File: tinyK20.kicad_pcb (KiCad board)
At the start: 2 copper layers, 45.8 x 73.7 mm, 78 parts, among them CON1 USB-MINI-B, P1 CONN_1, P10 CONN_1, P11 CONN_1, P12 CONN_1, P13 CONN_1, P14 CONN_1, P15 CONN_1, P16 CONN_1, P17 CONN_1, P18 CONN_1, P19 CONN_1, P2 CONN_1, P20 CONN_1, P21 CONN_1, P22 CONN_1, P23 CONN_1, P24 CONN_1, P25 CONN_1, P26 CONN_1, P27 CONN_1, P28 CONN_1, P29 CONN_1, P3 CONN_1, P30 CONN_1, P31 CONN_1, P32 CONN_1, P33 CONN_1, P34 CONN_1, P35 CONN_5X2, P36 CONN_1, P37 CONN_1, P38 CONN_5X2, P4 CONN_1, P41 CONN_1, P5 CONN_1, P6 CONN_1, P7 CONN_1, P8 CONN_1, P9 CONN_1, SW1 SW_PUSH, U1 MK20DX128VFT5, U2 LT1129CST-3.3, U3 74LS126, X3 MOLEX-MICRO-SD, Y1 Crystal, Y2 Crystal_Small

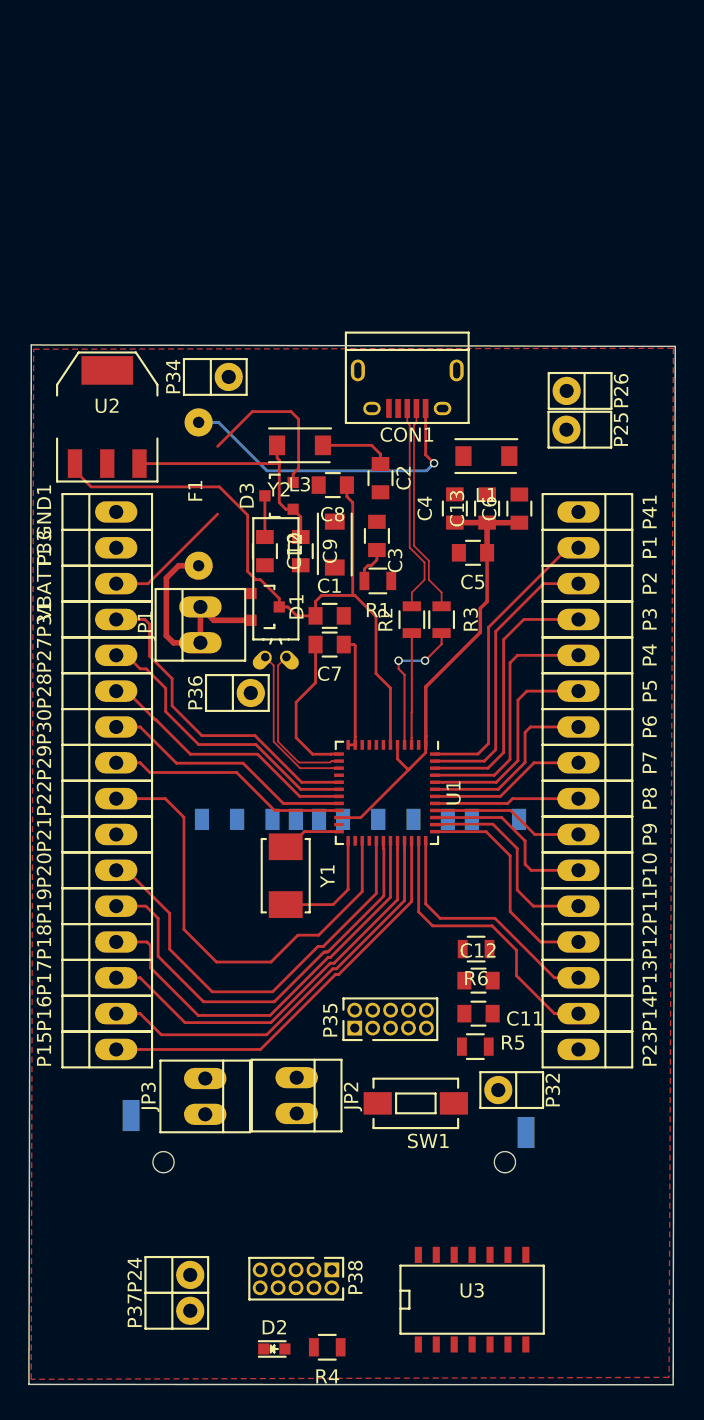
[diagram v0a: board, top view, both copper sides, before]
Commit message: Simplify the board
Remove all breakout pin headers
remove SD card connector
redo the PCB layout
change the debug connector to through hole 1.27mm
change the resistor footprints to handsoldering ones
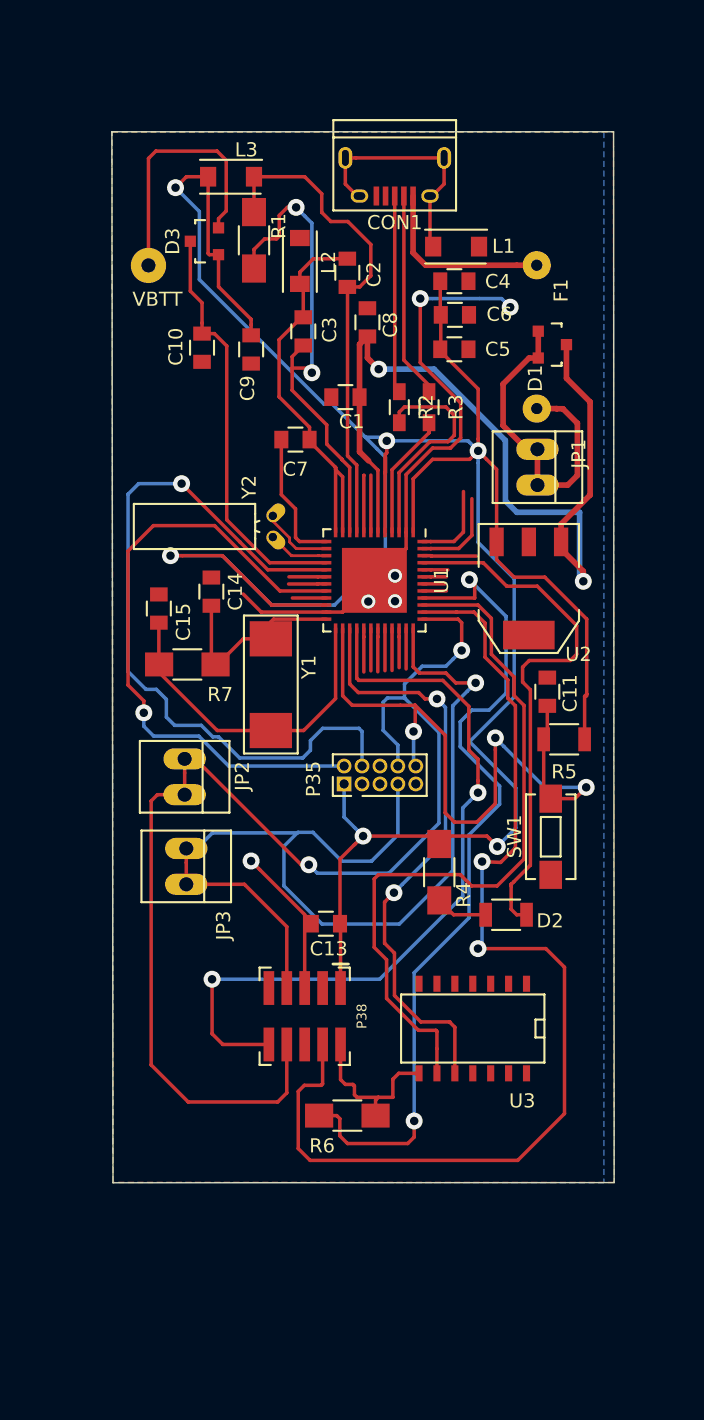
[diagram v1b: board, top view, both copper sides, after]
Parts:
- removed C12: 2.2u, Capacitors_SMD:C_0805
- removed GND1, P1, P10, P11, P12, P13, P14, P15, P16, P17, P18, P19, P2, P20, P21, P22, P23, P27, P28, P29, P3, P30, P31, P33, P4, P41, P5, P6, P7, P8, P9, VBATT1: CONN_1, Connect:PIN1
- removed P24, P25, P26, P32, P34, P36, P37: CONN_1, Connect:PINC
- removed X3: MOLEX-MICRO-SD, Connect:SD_Card_Receptacle
- added C14: 22nF, Capacitors_SMD:C_0805, F.Cu at (63.2, 61.9)
- added C15: 22nF, Capacitors_SMD:C_0805, F.Cu at (59.5, 63.1)
- added R7: 1M, Resistors_SMD:R_1206_HandSoldering, F.Cu at (61.5, 67.1)
- added VBTT: CONN_1, Wire_Pads:SolderWirePad_single_1mmDrill, F.Cu at (58.8, 38.8)
- D2: footprint LEDs:LED_0603 -> Resistors_SMD:R_1206
- P38: footprint Pin_Headers:Pin_Header_Straight_2x05_Pitch1.27mm -> Connect:CONN-2x5-1.27-SMT
- R1, R4, R6: footprint Resistors_SMD:R_0805 -> Resistors_SMD:R_1206_HandSoldering
- R2, R3: footprint Resistors_SMD:R_0805 -> Resistors_SMD:R_0603_HandSoldering
- R5: footprint Resistors_SMD:R_0805 -> Resistors_SMD:R_1206
- Y1: footprint Crystals:ABM3 -> Housings_DFN_QFN:ABM3
- moved D2 34.9 mm to (84.1, 84.8)
- moved R4 34.6 mm to (79.4, 81.8), turned to 270 degrees
- moved U2 32.3 mm to (85.7, 61.7), turned to 180 degrees
- moved C13 31.6 mm to (71.4, 85.5), turned to 180 degrees
- moved D1 27.6 mm to (87.4, 44.4)
- moved F1 26.4 mm to (86.3, 38.8)
- moved JP1 26.4 mm to (86.3, 53.1), turned to 270 degrees
- moved R1 25.7 mm to (66.3, 37.0), turned to 270 degrees
- moved JP2 24.0 mm to (61.3, 75.1)
- moved C11 23.3 mm to (87.0, 69.0), turned to 90 degrees
- moved R5 22.7 mm to (88.2, 72.4), turned to 180 degrees
- moved SW1 21.2 mm to (87.3, 79.3), turned to 90 degrees
- moved L2 20.3 mm to (69.5, 38.5), turned to 270 degrees
- moved L3 19.7 mm to (64.6, 32.5)
- moved U3 19.0 mm to (81.8, 93.0), turned to 180 degrees
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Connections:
- JP2 pad 1: Net-(JP2-Pad1) -> UART1_TX
- JP3 pad 1: Net-(JP3-Pad1) -> UART1_RX
- P38 pad 3: Net-(P38-Pad3) -> GND
- P38 pad 5: Net-(P38-Pad3) -> GND
- U1 pad 18: Net-(P27-Pad1) -> (no net)
- U1 pad 19: Net-(P28-Pad1) -> (no net)
- U1 pad 21: Net-(P29-Pad1) -> (no net)
- U1 pad 29: Net-(P20-Pad1) -> (no net)
- U1 pad 30: Net-(P19-Pad1) -> (no net)
- U1 pad 31: Net-(P18-Pad1) -> (no net)
- U1 pad 32: Net-(P17-Pad1) -> (no net)
- U1 pad 33: PTC0 -> (no net)
- U1 pad 34: PTC1 -> (no net)
- U1 pad 35: Net-(P14-Pad1) -> (no net)
- U1 pad 36: Net-(JP3-Pad1) -> UART1_RX
- U1 pad 37: Net-(JP2-Pad1) -> UART1_TX
- U1 pad 41: Net-(P8-Pad1) -> (no net)
- U1 pad 42: Net-(P7-Pad1) -> (no net)
- U1 pad 43: Net-(P6-Pad1) -> (no net)
- U1 pad 44: Net-(P5-Pad1) -> (no net)
- U1 pad 46: Net-(P3-Pad1) -> (no net)
- U1 pad 47: Net-(P2-Pad1) -> (no net)
- U1 pad 48: Net-(P1-Pad1) -> (no net)
- U1 pad 7: Net-(P25-Pad1) -> (no net)
- U1 pad 8: Net-(P26-Pad1) -> (no net)
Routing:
- net 3V3: track 50.4 -> 200.1 mm, vias 0 -> 6
- net UART1_TX: track 0.00 -> 88.4 mm, vias 0 -> 2
- net UART1_RX: track 0.00 -> 76.4 mm, vias 0 -> 1
- net PTC5: track 14.3 -> 77.3 mm, vias 0 -> 2
- net (no net): track 0.00 -> 59.9 mm
- net GND: track 0.00 -> 57.8 mm, vias 0 -> 6
- net PTB1: track 0.00 -> 54.9 mm, vias 0 -> 2
- net RESET: track 0.00 -> 50.6 mm, vias 0 -> 3
- net PTC7: track 10.9 -> 59.9 mm, vias 0 -> 2
- net SWD_CLK: track 11.6 -> 53.1 mm, vias 0 -> 1
- net PTC6: track 12.7 -> 51.5 mm
- net Net-(C3-Pad1): track 2.70 -> 35.4 mm, vias 0 -> 2
- net Net-(C2-Pad1): track 5.04 -> 35.5 mm
- net Net-(P19-Pad1): track 30.4 -> 0.00 mm
- net Net-(P20-Pad1): track 30.1 -> 0.00 mm
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- added copper zone on B.Cu, net GND
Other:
- board size 45.8 x 73.7 mm -> 35.6 x 74.5 mm
- net class Default: trace_width 0.4 -> 0.25; via_dia 0.6 -> 1.2; via_drill 0.4 -> 0.6
- net class diff: clearance 0.1 -> 0.2; via_dia 0.4 -> 1.2; via_drill 0.3 -> 0.6
- rule trace_min: 0.1 -> 0.006
- rule via_min_drill: 0.3 -> 0.013
- rule via_min_size: 0.4 -> 0.027

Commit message: Add breakout headers and reroute the whole PCB board
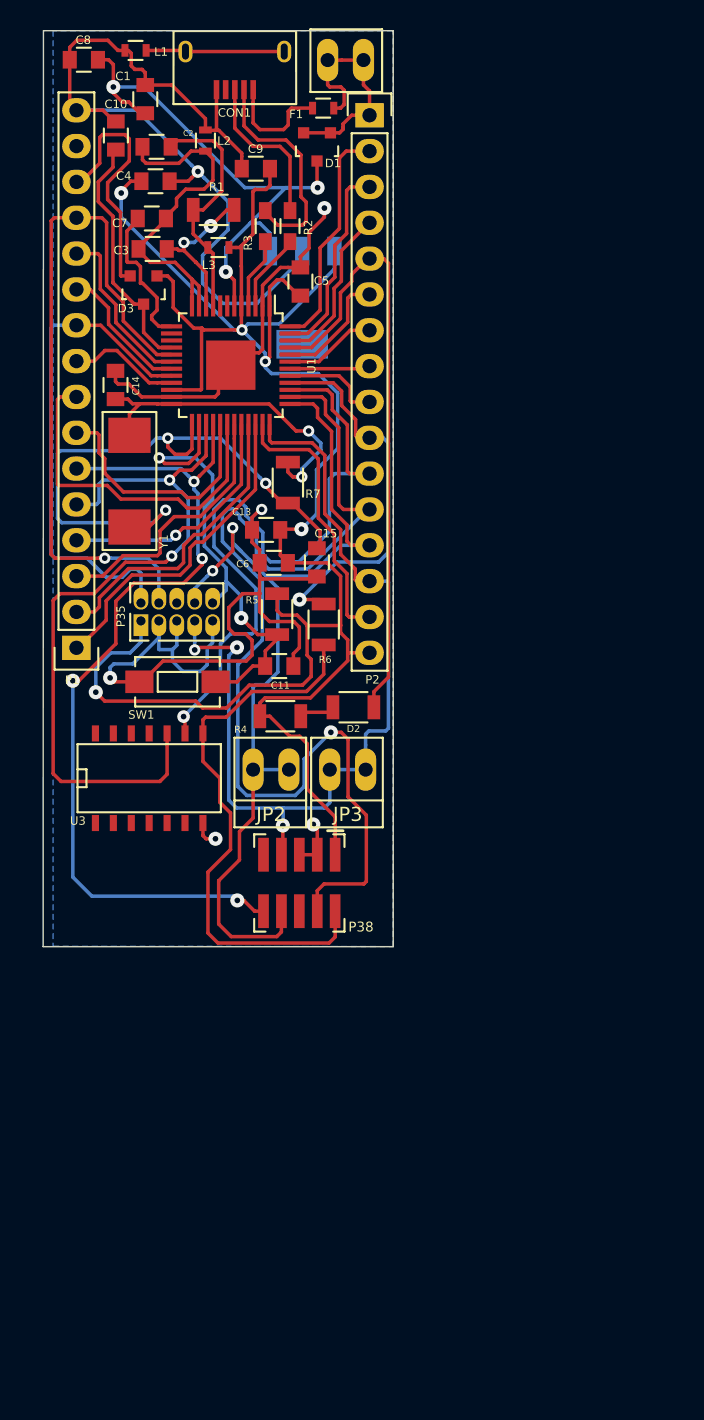
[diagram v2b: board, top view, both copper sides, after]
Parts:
- removed VBTT: CONN_1, Wire_Pads:SolderWirePad_single_1mmDrill
- removed Y2: Crystal_Small, Crystals:Crystal_Round_Horizontal_3mm_BigPad
- added P1: CONN_01X16, Pin_Headers:Pin_Header_Straight_1x16, F.Cu at (53.7, 65.9)
- added P2: CONN_01X16, Pin_Headers:Pin_Header_Straight_1x16, F.Cu at (74.4, 28.2)
- C10: value 100n -> C
- CON1: value USB-MINI-B -> USB-MICRO-B
- F1: footprint Wire_Connections_Bridges:WireConnection_0.80mmDrill -> Resistors_SMD:R_0603
- L1, L2, L3: footprint Inductors_NEOSID:Neosid_Inductor_SM1206 -> Resistors_SMD:R_0603
- P38: footprint Connect:CONN-2x5-1.27-SMT -> Pin_Headers:CONN-2x5-1.27-SMT
- R1, R4, R6, R7: footprint Resistors_SMD:R_1206_HandSoldering -> Resistors_SMD:R_1206
- U1: footprint Housings_DFN_QFN:QFN-48-1EP_7x7mm_Pitch0.5mm -> Housings_QFP:TQFP-48-1EP_7x7mm_Pitch0.5mm
- U2: moved to B.Cu
- moved R6 34.8 mm to (71.2, 64.3), turned to 270 degrees
- moved JP1 31.9 mm to (72.7, 24.3), turned to 0 degrees
- moved U3 29.2 mm to (58.8, 75.0), turned to 0 degrees
- moved SW1 28.6 mm to (60.8, 68.3), turned to 0 degrees
- moved C13 28.2 mm to (67.1, 57.6)
- moved C8 27.4 mm to (54.2, 24.2), turned to 180 degrees
- moved L1 26.6 mm to (57.9, 23.6), turned to 0 degrees
- moved U2 26.1 mm to (69.7, 41.1), turned to 0 degrees
- moved C1 25.4 mm to (58.5, 27.0), turned to 90 degrees
- moved C4 22.3 mm to (59.3, 32.8)
- moved R5 22.2 mm to (67.9, 63.5), turned to 270 degrees
- moved D1 21.8 mm to (70.7, 30.4), turned to 180 degrees
- moved C6 21.8 mm to (67.7, 59.9), turned to 180 degrees
- moved C11 19.1 mm to (68.0, 67.2), turned to 0 degrees
- moved F1 18.8 mm to (71.2, 27.7), turned to 0 degrees
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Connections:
- net /D+ renamed D+
- net /D- renamed D-
- net LED renamed PTD4
- net Net-(D1-Pad1) renamed 5V
- net SWD_CLK renamed PTA0
- net SWD_IO renamed PTA3
- D3 pad 2: Net-(D3-Pad2) -> VBATT
- U1 pad 14: /xtal_P -> (no net)
- U1 pad 15: /xtal_N -> (no net)
- U1 pad 18: (no net) -> PTA1
- U1 pad 19: (no net) -> PTA2
- U1 pad 21: (no net) -> PTA4
- U1 pad 29: (no net) -> PTB2
- U1 pad 30: (no net) -> PTB3
- U1 pad 31: (no net) -> PTB16
- U1 pad 32: (no net) -> PTB17
- U1 pad 33: (no net) -> PTC0
- U1 pad 34: (no net) -> PTC1
- U1 pad 35: (no net) -> PTC2
- U1 pad 41: (no net) -> PTD0
- U1 pad 42: (no net) -> PTD1
- U1 pad 43: (no net) -> PTD2
- U1 pad 44: (no net) -> PTD3
- U1 pad 46: (no net) -> PTD5
- U1 pad 47: (no net) -> PTD6
- U1 pad 48: (no net) -> PTD7
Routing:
- net GND: track 57.8 -> 150.8 mm
- net (no net): track 59.9 -> 0.00 mm
- net 3V3: track 200.1 -> 153.0 mm, vias 6 -> 5
- net PTC7: track 59.9 -> 27.3 mm, vias 2 -> 1
- net Net-(P38-Pad2): track 11.8 -> 39.9 mm
- net PTB3: track 0.00 -> 24.9 mm
- net Net-(C3-Pad1): track 35.4 -> 10.9 mm
- net PTC1: track 0.00 -> 23.6 mm
- net Vregin: track 62.2 -> 39.5 mm, vias 2 -> 3
- net PTC0: track 0.00 -> 21.6 mm
- net /x+: track 23.7 -> 43.5 mm, vias 0 -> 3
- net PTC2: track 0.00 -> 19.3 mm
- net PTB16: track 0.00 -> 19.1 mm
- net Net-(D3-Pad2): track 18.6 -> 0.00 mm
- net Net-(C2-Pad1): track 35.5 -> 17.0 mm
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- removed copper zone on F.Cu, net GND
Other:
- board size 35.6 x 74.5 mm -> 24.8 x 64.9 mm
- net class Default: via_dia 1.2 -> 0.6; via_drill 0.6 -> 0.4
- net class diff removed
- rule trace_min: 0.006 -> 0.2
- rule via_min_drill: 0.013 -> 0.3
- rule via_min_size: 0.027 -> 0.4

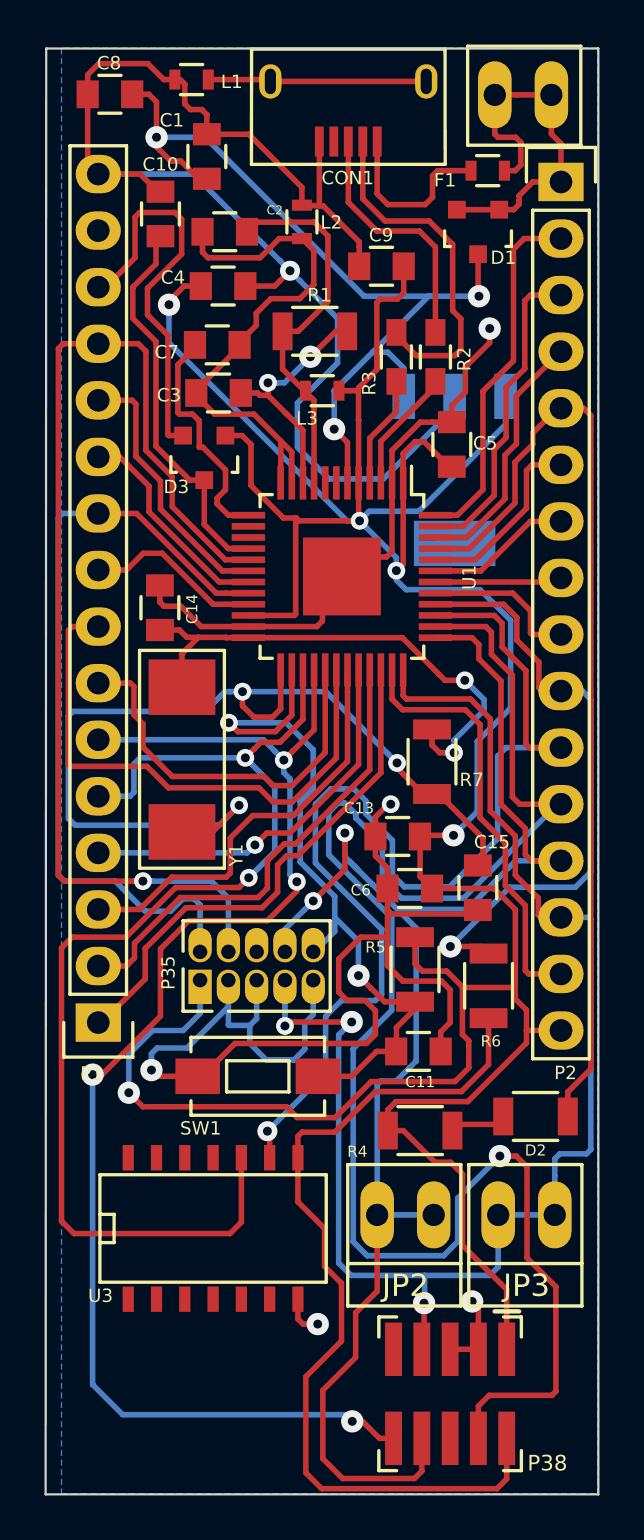
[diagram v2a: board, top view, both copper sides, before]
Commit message: Make the board smaller
Switch the ABM2 crystal with a smaller Murata CSTE
Switch the debug line driver chip with a smaller footprint one
Adjust pin headers hopefully to breadboard friendly
Remove Jumpers on UART lines
Remove the 1Mohm resistor and two capacitors for the crystal. Not needed
Resize the entire board downwards and re-route the traces
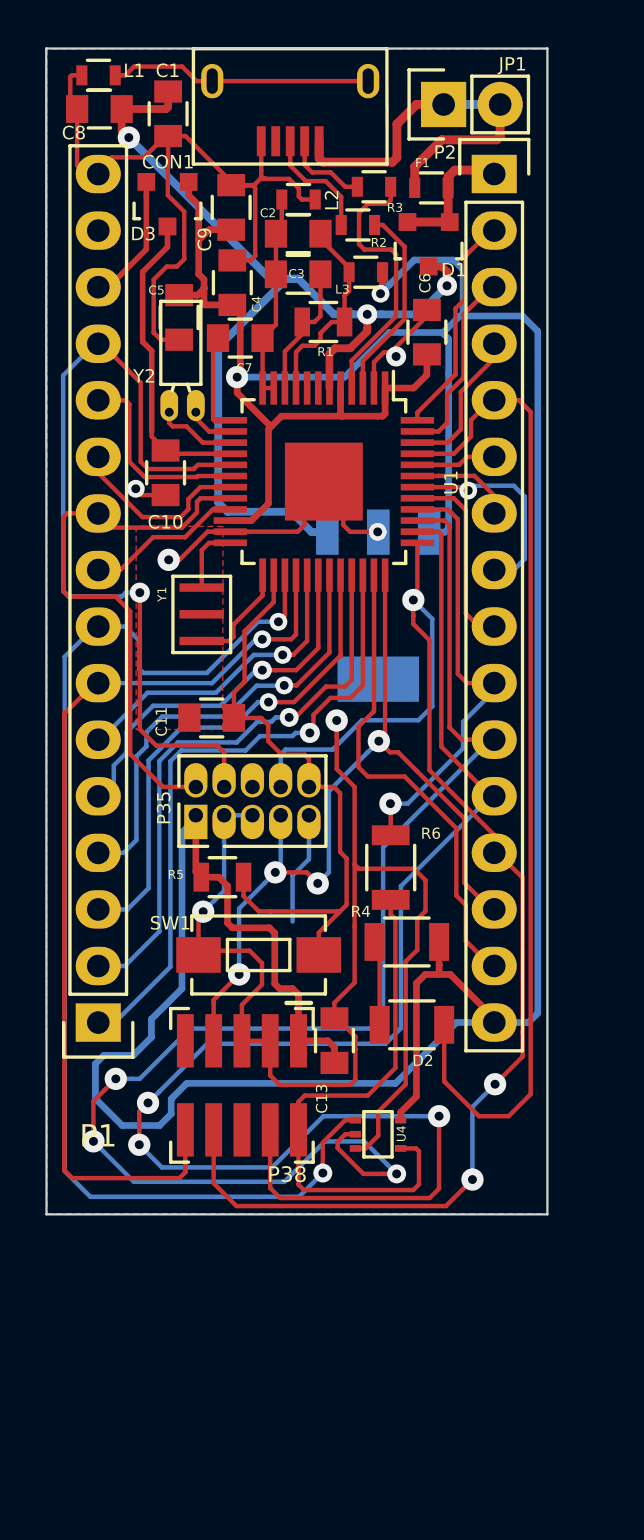
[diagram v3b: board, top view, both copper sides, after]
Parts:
- removed C14, C15: 22nF, Capacitors_SMD:C_0805
- removed JP2, JP3: JUMPER_F, Connect:PINHEAD1-2
- removed R7: 1M, Resistors_SMD:R_1206
- removed U3: 74LS126, SMD_Packages:SOIC-14_N
- added U4: 74AHC1G125, TO_SOT_Packages_SMD:SOT-353, F.Cu at (66.2, 70.9)
- added Y2: 32.768kHz, Crystals:Crystal_Round_Horizontal_2mm, F.Cu at (57.4, 38.5)
- C10: value C -> 100nF
- JP1: footprint Connect:PINHEAD1-2 -> Pin_Headers:Pin_Header_Straight_1x02
- R1, R5: footprint Resistors_SMD:R_1206 -> Resistors_SMD:R_0805
- R2, R3: footprint Resistors_SMD:R_0603_HandSoldering -> Resistors_SMD:R_0603
- Y1: value Crystal -> 8MHz; footprint Housings_DFN_QFN:ABM3 -> Crystals:CERALOCK-CSTCE8M00G15L99-R0
- moved C6 25.0 mm to (68.4, 34.9), turned to 90 degrees
- moved C11 17.6 mm to (58.8, 52.2), turned to 180 degrees
- moved P38 16.7 mm to (60.1, 68.7)
- moved C5 13.5 mm to (57.3, 34.3), turned to 270 degrees
- moved C10 11.6 mm to (56.7, 41.2), turned to 270 degrees
- moved D3 11.5 mm to (56.8, 29.2)
- moved C13 9.60 mm to (64.3, 66.7), turned to 90 degrees
- moved R5 9.59 mm to (59.2, 59.4), turned to 0 degrees
- moved R4 8.49 mm to (67.5, 62.3), turned to 180 degrees
- moved R3 7.71 mm to (66.1, 28.4), turned to 0 degrees
- moved P35 7.41 mm to (58.1, 56.6)
- moved C9 7.25 mm to (59.6, 29.3), turned to 90 degrees
- moved U2 6.99 mm to (66.2, 47.2)
- moved D2 6.91 mm to (67.8, 66.0)
- moved R6 6.89 mm to (66.8, 59.0)
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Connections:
- JP1 pad 1: 5V -> Vreg
- JP1 pad 2: 5V -> Vreg
- P1 pad 3: PTB16 -> PTB17
- P1 pad 4: PTB17 -> PTB16
- P1 pad 5: PTB0 -> PTB3
- P1 pad 6: PTB1 -> PTB2
- P1 pad 7: PTB2 -> PTB1
- P1 pad 8: PTB3 -> PTB0
- U1 pad 14: (no net) -> Net-(U1-Pad14)
- U1 pad 15: (no net) -> Net-(U1-Pad15)
- Y1 pad 2: /x+ -> GND
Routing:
- net /x+: track 43.5 -> 4.81 mm, vias 3 -> 0
- net GND: track 150.8 -> 120.6 mm
- net UART1_RX: track 64.3 -> 38.6 mm, vias 3 -> 4
- net /x-: track 23.2 -> 3.10 mm, vias 2 -> 0
- net PTB1: track 62.4 -> 42.6 mm, vias 4 -> 1
- net Net-(P38-Pad2): track 39.9 -> 24.3 mm
- net Net-(C2-Pad2): track 24.7 -> 9.33 mm
- net PTC6: track 50.0 -> 63.9 mm, vias 1 -> 3
- net PTA0: track 50.2 -> 37.8 mm
- net D-: track 15.8 -> 3.83 mm
- net VBATT: track 17.7 -> 5.89 mm
- net 5V: track 17.0 -> 6.40 mm
- net PTA3: track 35.8 -> 25.4 mm
- net 3V3: track 153.0 -> 162.9 mm, vias 5 -> 2
- net Vreg: track 7.96 -> 17.7 mm
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- added copper zone on F.Cu, net GND
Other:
- board size 24.8 x 64.9 mm -> 22.5 x 52.3 mm
- net class Default: clearance 0.2 -> 0.16; trace_width 0.25 -> 0.2
- net class POWER added: clearance 0.2, trace_width 0.3, via_dia 0.6, via_drill 0.4
- rule trace_clearance: 0.2 -> 0.16
